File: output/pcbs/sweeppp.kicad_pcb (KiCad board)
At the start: 2 copper layers, 136.5 x 111 mm, 57 parts

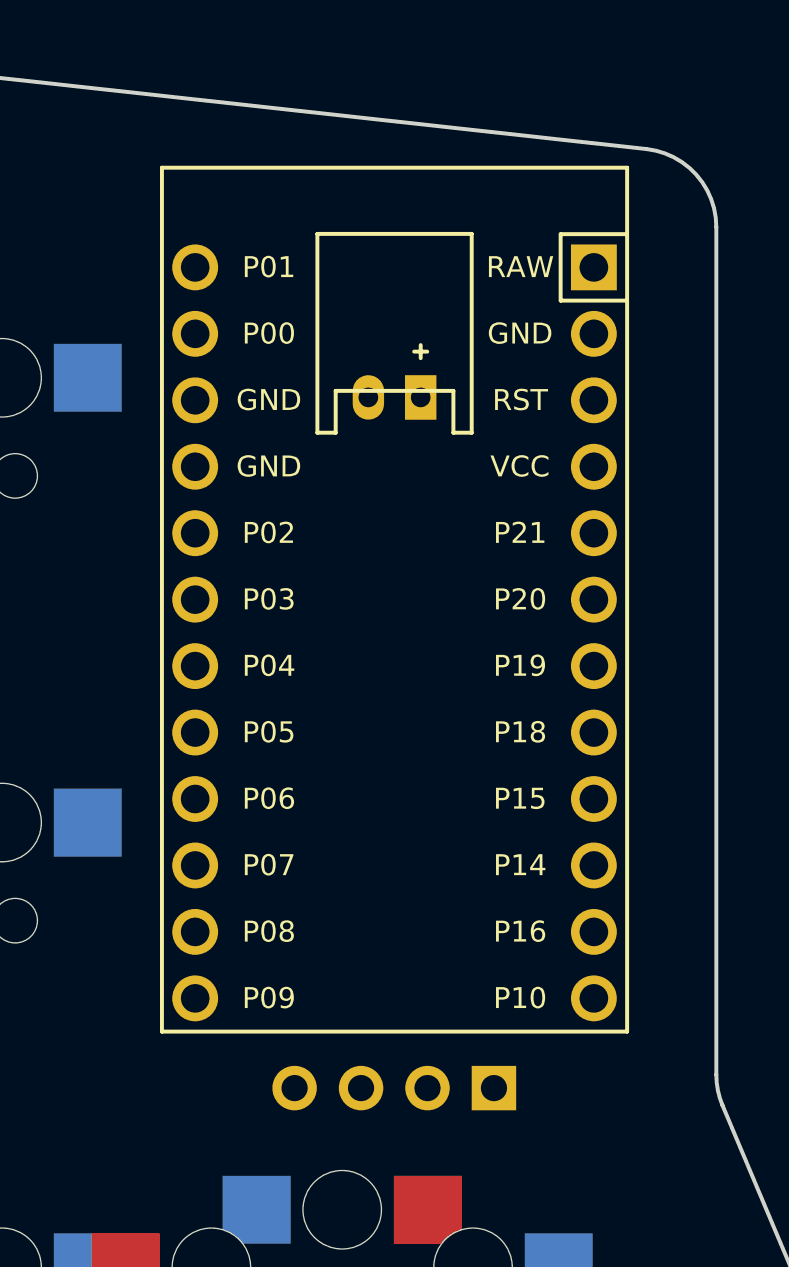
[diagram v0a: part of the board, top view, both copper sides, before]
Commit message: switched to nice nano and nice view
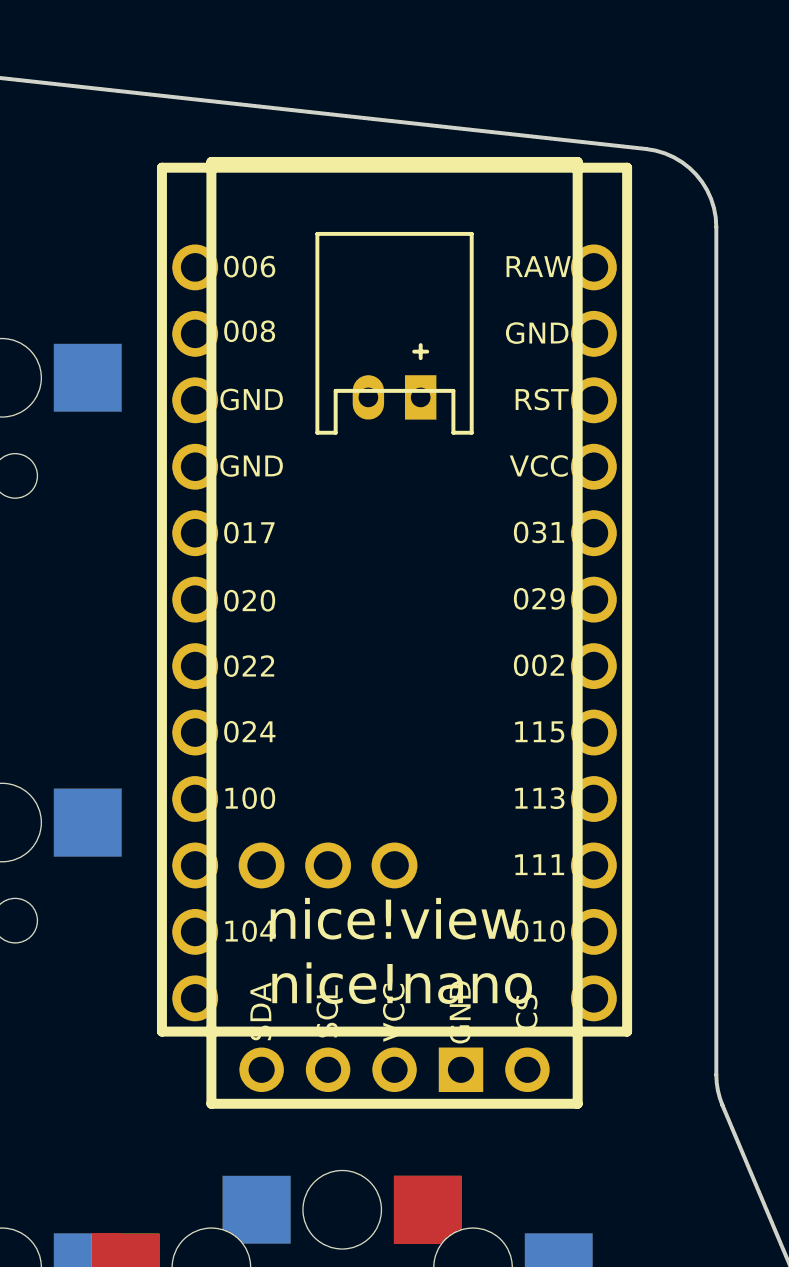
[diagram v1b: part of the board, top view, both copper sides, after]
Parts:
- removed OLED1: OLED, lib:OLED_headers
- added niceView1: niceView, lib:niceView_headers, F.Cu at (192.0, 63.5)
- MCU1: value (none) -> nice_nano; footprint ProMicro -> nice_nano
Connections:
- net P0 renamed P010
- net P1 renamed P009
- net P19 renamed P022
- net P20 renamed P020
- net P21 renamed P017
- MCU1 pad 1: RAW -> P006
- MCU1 pad 10: P14 -> P011
- MCU1 pad 11: P16 -> P104
- MCU1 pad 12: P10 -> P106
- MCU1 pad 15: GND -> P111
- MCU1 pad 16: GND -> P113
- MCU1 pad 17: P2 -> P115
- MCU1 pad 18: P3 -> P002
- MCU1 pad 19: P4 -> P029
- MCU1 pad 2: GND -> P008
- MCU1 pad 20: P5 -> P031
- MCU1 pad 21: P6 -> VCC
- MCU1 pad 22: P7 -> RST
- MCU1 pad 23: P8 -> GND
- MCU1 pad 24: P9 -> RAW
- MCU1 pad 3: RST -> GND
- MCU1 pad 4: VCC -> GND
- MCU1 pad 8: P18 -> P024
- MCU1 pad 9: P15 -> P100

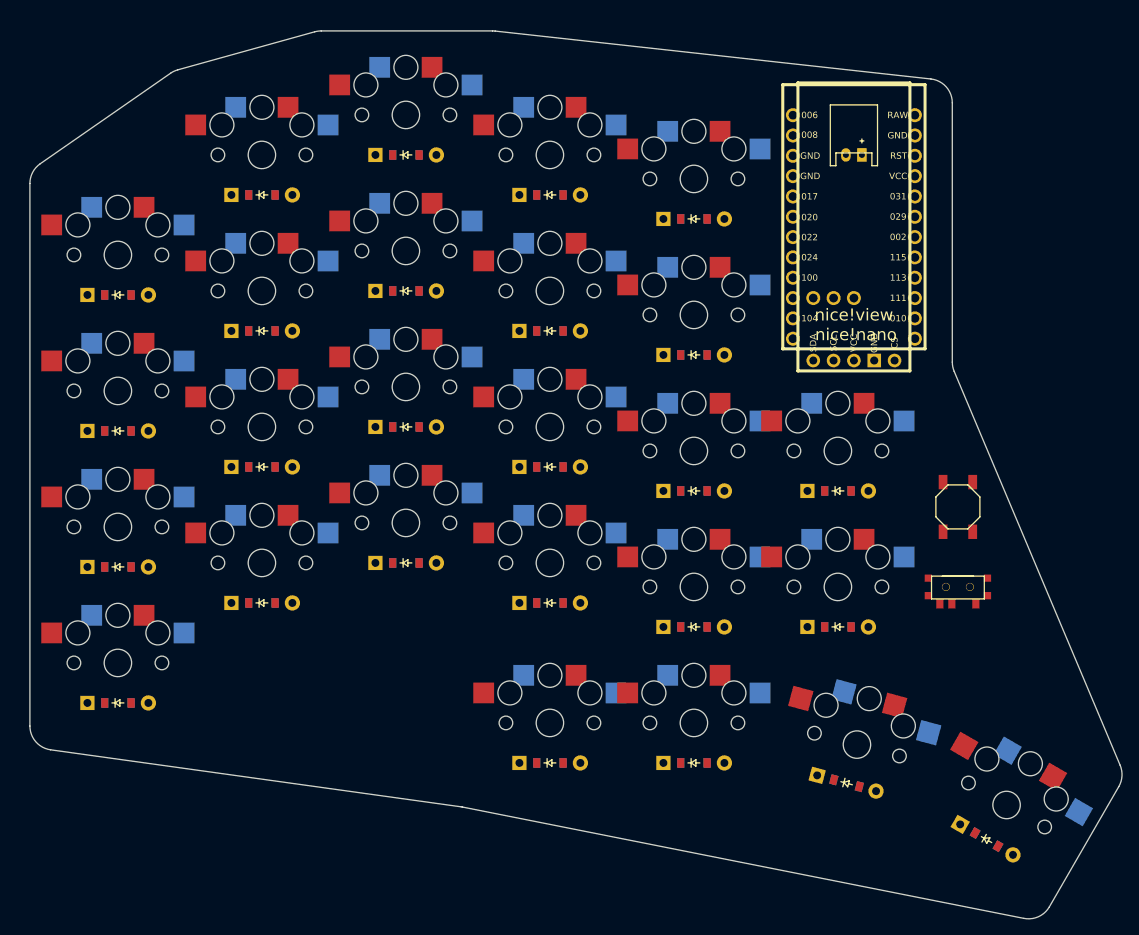
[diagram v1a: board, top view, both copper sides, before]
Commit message: moved the reset button and power switch adjusted outline
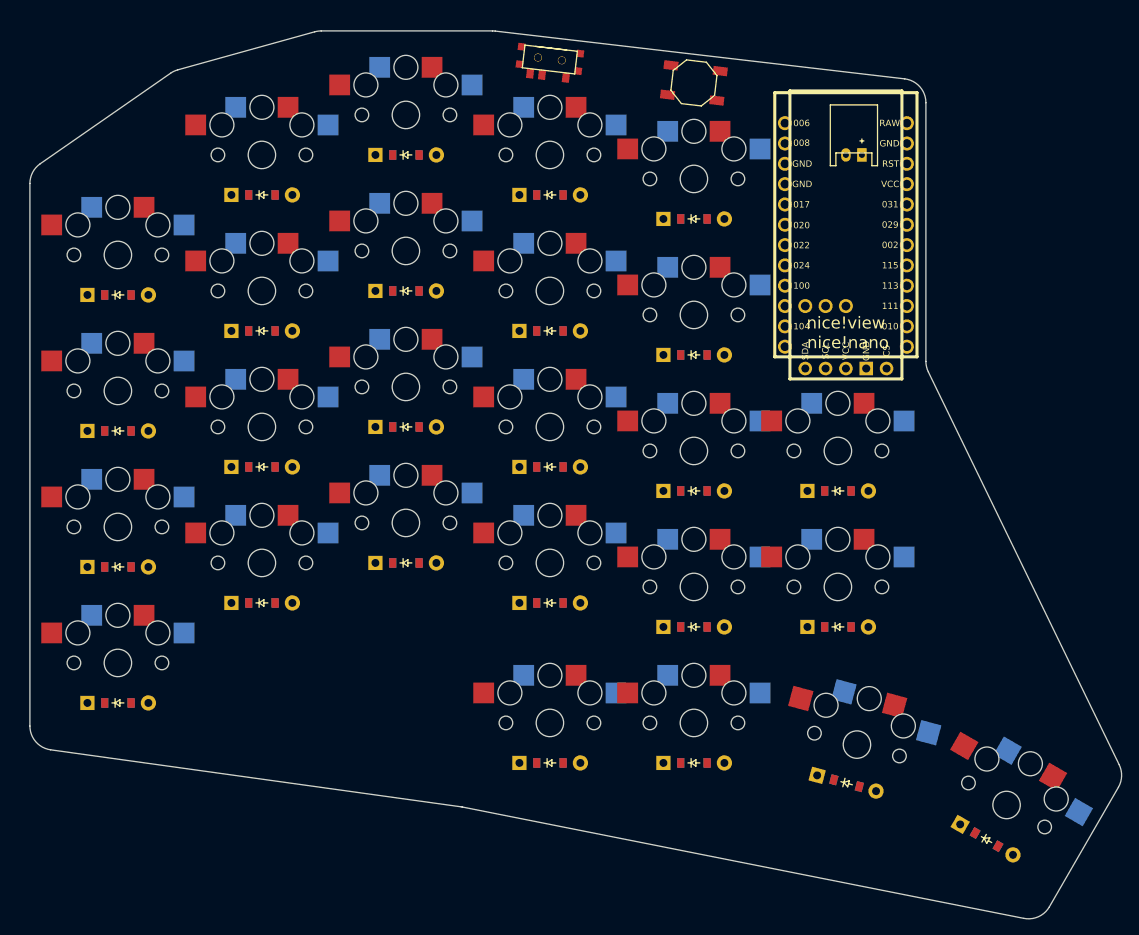
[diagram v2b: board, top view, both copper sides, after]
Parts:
- moved T1 83.4 mm to (154.0, 24.5), turned to -6.7 degrees
- moved B1 62.4 mm to (172.0, 27.5), turned to -6.7 degrees
- moved MCU1 1.41 mm to (191.0, 46.5)
- moved niceView1 1.41 mm to (191.0, 64.5)
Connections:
- D1 pad 1: P4 -> P022
- D10 pad 1: P5 -> P024
- D11 pad 1: P6 -> P100
- D12 pad 1: P7 -> P011
- D13 pad 1: P4 -> P022
- D14 pad 1: P5 -> P024
- D15 pad 1: P6 -> P100
- D16 pad 1: P7 -> P011
- D17 pad 1: P4 -> P022
- D18 pad 1: P5 -> P024
- D19 pad 1: P6 -> P100
- D2 pad 1: P5 -> P024
- D20 pad 1: P7 -> P011
- D21 pad 1: P4 -> P022
- D22 pad 1: P5 -> P024
- D23 pad 1: P8 -> P104
- D24 pad 1: P8 -> P104
- D25 pad 1: P8 -> P104
- D26 pad 1: P8 -> P104
- D3 pad 1: P6 -> P100
- D4 pad 1: P7 -> P011
- D5 pad 1: P4 -> P022
- D6 pad 1: P5 -> P024
- D7 pad 1: P6 -> P100
- D8 pad 1: P7 -> P011
- D9 pad 1: P4 -> P022
- S1 pad 1: P18 -> P115
- S10 pad 1: P14 -> P111
- S11 pad 1: P14 -> P111
- S12 pad 1: P14 -> P111
- S13 pad 1: P16 -> P010
- S14 pad 1: P16 -> P010
- S15 pad 1: P16 -> P010
- S16 pad 1: P16 -> P010
- S17 pad 1: P10 -> P009
- S18 pad 1: P10 -> P009
- S19 pad 1: P10 -> P009
- S2 pad 1: P18 -> P115
- S20 pad 1: P10 -> P009
- S21 pad 1: P9 -> P106
- S22 pad 1: P9 -> P106
- S23 pad 1: P14 -> P111
- S24 pad 1: P16 -> P010
- S25 pad 1: P10 -> P009
- S26 pad 1: P9 -> P106
- S3 pad 1: P18 -> P115
- S4 pad 1: P18 -> P115
- S5 pad 1: P15 -> P113
- S6 pad 1: P15 -> P113
- S7 pad 1: P15 -> P113
- S8 pad 1: P15 -> P113
- S9 pad 1: P14 -> P111
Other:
- outline, holes or cut-outs redrawn

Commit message: moved jstph
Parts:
- moved JST1 79.9 mm to (136.0, 93.5), turned to 0 degrees
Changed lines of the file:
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@@
         (descr "JST PH series connector, S2B-PH-K, side entry type, through hole, Datasheet: http://www.jst-mfg.com/product/pdf/eng/ePH.pdf")
         (tags "connector jst ph")
-        (at 192 36.5 180)
+        (at 136 93.5 0)
         (fp_text reference "JST1" (at 0 0) (layer F.SilkS) hide (effects (font (size 1.27 1.27) (thickness 0.15))))
         (fp_text value "" (at 0 0) (layer F.SilkS) hide (effects (font (size 1.27 1.27) (thickness 0.15))))
@@
         (fp_line (start -1 1.5) (end -1 2.0) (layer F.SilkS) (width 0.15))
         (fp_line (start -1.25 1.75) (end -0.75 1.75) (layer F.SilkS) (width 0.15))
-        (pad 1 thru_hole rect (at -1 0 180) (size 1.2 1.7) (drill 0.75) (layers *.Cu *.Mask) (net 54 "BAT"))
-        (pad 2 thru_hole oval (at 1 0 180) (size 1.2 1.7) (drill 0.75) (layers *.Cu *.Mask) (net 39 "GND"))
+        (pad 1 thru_hole rect (at -1 0 0) (size 1.2 1.7) (drill 0.75) (layers *.Cu *.Mask) (net 54 "BAT"))
+        (pad 2 thru_hole oval (at 1 0 0) (size 1.2 1.7) (drill 0.75) (layers *.Cu *.Mask) (net 39 "GND"))
     )
   (gr_line (start 89 107.88786971388888) (end 89 40.069101149999995) (angle 90) (layer Edge.Cuts) (width 0.15))

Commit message: Added mounting holes
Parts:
- added _1: , MountingHole_2.2mm_M2_Pad_Via, F.Cu at (100.0, 37.0)
- added _2: , MountingHole_2.2mm_M2_Pad_Via, F.Cu at (112.0, 109.0)
- added _3: , MountingHole_2.2mm_M2_Pad_Via, F.Cu at (179.0, 28.5)
- added _4: , MountingHole_2.2mm_M2_Pad_Via, F.Cu at (206.0, 102.5)
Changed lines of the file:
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@@
         (pad 2 thru_hole oval (at 1 0 0) (size 1.2 1.7) (drill 0.75) (layers *.Cu *.Mask) (net 39 "GND"))
+    )
+    (module "MountingHole_2.2mm_M2_Pad_Via" (version 20210722) (generator pcbnew) (layer "F.Cu")
+      (at 100 37 0)
+      (fp_text reference "_1" (at 0 -3.2) (layer "F.SilkS") hide
+        (effects (font (size 1 1) (thickness 0.15)))
+      )
+      (fp_circle (center 0 0) (end 2.45 0) (layer "F.CrtYd") (width 0.05) (fill none))
+      (pad "1" thru_hole circle locked (at 1.166726 1.166726) (size 0.7 0.7) (drill 0.4) (layers *.Cu *.Mask))
+      (pad "1" thru_hole circle locked (at 0 0) (size 4.4 4.4) (drill 2.2) (layers *.Cu *.Mask))
+      (pad "1" thru_hole circle locked (at 0 1.65) (size 0.7 0.7) (drill 0.4) (layers *.Cu *.Mask))
+      (pad "1" thru_hole circle locked (at 1.166726 -1.166726) (size 0.7 0.7) (drill 0.4) (layers *.Cu *.Mask))
+      (pad "1" thru_hole circle locked (at -1.65 0) (size 0.7 0.7) (drill 0.4) (layers *.Cu *.Mask))
+      (pad "1" thru_hole circle locked (at -1.166726 -1.166726) (size 0.7 0.7) (drill 0.4) (layers *.Cu *.Mask))
+      (pad "1" thru_hole circle locked (at -1.166726 1.166726) (size 0.7 0.7) (drill 0.4) (layers *.Cu *.Mask))
+      (pad "1" thru_hole circle locked (at 1.65 0) (size 0.7 0.7) (drill 0.4) (layers *.Cu *.Mask))
+      (pad "1" thru_hole circle locked (at 0 -1.65) (size 0.7 0.7) (drill 0.4) (layers *.Cu *.Mask))
+    )
+    (module "MountingHole_2.2mm_M2_Pad_Via" (version 20210722) (generator pcbnew) (layer "F.Cu")
+      (at 112 109 0)
+      (fp_text reference "_2" (at 0 -3.2) (layer "F.SilkS") hide
+        (effects (font (size 1 1) (thickness 0.15)))
+      )
+      (fp_circle (center 0 0) (end 2.45 0) (layer "F.CrtYd") (width 0.05) (fill none))
+      (pad "1" thru_hole circle locked (at 1.166726 1.166726) (size 0.7 0.7) (drill 0.4) (layers *.Cu *.Mask))
+      (pad "1" thru_hole circle locked (at 0 0) (size 4.4 4.4) (drill 2.2) (layers *.Cu *.Mask))
+      (pad "1" thru_hole circle locked (at 0 1.65) (size 0.7 0.7) (drill 0.4) (layers *.Cu *.Mask))
+      (pad "1" thru_hole circle locked (at 1.166726 -1.166726) (size 0.7 0.7) (drill 0.4) (layers *.Cu *.Mask))
+      (pad "1" thru_hole circle locked (at -1.65 0) (size 0.7 0.7) (drill 0.4) (layers *.Cu *.Mask))
+      (pad "1" thru_hole circle locked (at -1.166726 -1.166726) (size 0.7 0.7) (drill 0.4) (layers *.Cu *.Mask))
+      (pad "1" thru_hole circle locked (at -1.166726 1.166726) (size 0.7 0.7) (drill 0.4) (layers *.Cu *.Mask))
+      (pad "1" thru_hole circle locked (at 1.65 0) (size 0.7 0.7) (drill 0.4) (layers *.Cu *.Mask))
+      (pad "1" thru_hole circle locked (at 0 -1.65) (size 0.7 0.7) (drill 0.4) (layers *.Cu *.Mask))
+    )
+    (module "MountingHole_2.2mm_M2_Pad_Via" (version 20210722) (generator pcbnew) (layer "F.Cu")
+      (at 179 28.5 0)
+      (fp_text reference "_3" (at 0 -3.2) (layer "F.SilkS") hide
+        (effects (font (size 1 1) (thickness 0.15)))
+      )
+      (fp_circle (center 0 0) (end 2.45 0) (layer "F.CrtYd") (width 0.05) (fill none))
+      (pad "1" thru_hole circle locked (at 1.166726 1.166726) (size 0.7 0.7) (drill 0.4) (layers *.Cu *.Mask))
+      (pad "1" thru_hole circle locked (at 0 0) (size 4.4 4.4) (drill 2.2) (layers *.Cu *.Mask))
+      (pad "1" thru_hole circle locked (at 0 1.65) (size 0.7 0.7) (drill 0.4) (layers *.Cu *.Mask))
+      (pad "1" thru_hole circle locked (at 1.166726 -1.166726) (size 0.7 0.7) (drill 0.4) (layers *.Cu *.Mask))
+      (pad "1" thru_hole circle locked (at -1.65 0) (size 0.7 0.7) (drill 0.4) (layers *.Cu *.Mask))
+      (pad "1" thru_hole circle locked (at -1.166726 -1.166726) (size 0.7 0.7) (drill 0.4) (layers *.Cu *.Mask))
+      (pad "1" thru_hole circle locked (at -1.166726 1.166726) (size 0.7 0.7) (drill 0.4) (layers *.Cu *.Mask))
+      (pad "1" thru_hole circle locked (at 1.65 0) (size 0.7 0.7) (drill 0.4) (layers *.Cu *.Mask))
+      (pad "1" thru_hole circle locked (at 0 -1.65) (size 0.7 0.7) (drill 0.4) (layers *.Cu *.Mask))
+    )
+    (module "MountingHole_2.2mm_M2_Pad_Via" (version 20210722) (generator pcbnew) (layer "F.Cu")
+      (at 206 102.5 0)
+      (fp_text reference "_4" (at 0 -3.2) (layer "F.SilkS") hide
+        (effects (font (size 1 1) (thickness 0.15)))
+      )
+      (fp_circle (center 0 0) (end 2.45 0) (layer "F.CrtYd") (width 0.05) (fill none))
+      (pad "1" thru_hole circle locked (at 1.166726 1.166726) (size 0.7 0.7) (drill 0.4) (layers *.Cu *.Mask))
+      (pad "1" thru_hole circle locked (at 0 0) (size 4.4 4.4) (drill 2.2) (layers *.Cu *.Mask))
+      (pad "1" thru_hole circle locked (at 0 1.65) (size 0.7 0.7) (drill 0.4) (layers *.Cu *.Mask))
+      (pad "1" thru_hole circle locked (at 1.166726 -1.166726) (size 0.7 0.7) (drill 0.4) (layers *.Cu *.Mask))
+      (pad "1" thru_hole circle locked (at -1.65 0) (size 0.7 0.7) (drill 0.4) (layers *.Cu *.Mask))
+      (pad "1" thru_hole circle locked (at -1.166726 -1.166726) (size 0.7 0.7) (drill 0.4) (layers *.Cu *.Mask))
+      (pad "1" thru_hole circle locked (at -1.166726 1.166726) (size 0.7 0.7) (drill 0.4) (layers *.Cu *.Mask))
+      (pad "1" thru_hole circle locked (at 1.65 0) (size 0.7 0.7) (drill 0.4) (layers *.Cu *.Mask))
+      (pad "1" thru_hole circle locked (at 0 -1.65) (size 0.7 0.7) (drill 0.4) (layers *.Cu *.Mask))
     )
   (gr_line (start 89 107.88786971388888) (end 89 40.069101149999995) (angle 90) (layer Edge.Cuts) (width 0.15))

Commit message: Added pins for nice!view
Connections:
- niceView1 pad 1: (no net) -> P002
- niceView1 pad 4: P3 -> P020
- niceView1 pad 5: P2 -> P017
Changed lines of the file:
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@@
 (net 50 "P102")
 (net 51 "P107")
-(net 52 "P2")
-(net 53 "P3")
-(net 54 "BAT")
+(net 52 "BAT")
   (net_class Default "This is the default net class."
     (clearance 0.2)
@@
 (add_net "P102")
 (add_net "P107")
-(add_net "P2")
-(add_net "P3")
 (add_net "BAT")
   )
@@
         (fp_text user CS (at 3.5 5.08 270) (layer B.SilkS) (effects (font (size 0.8 0.8) (thickness 0.15)) (justify mirror)))
         (fp_text user nice!view (at 7 0 360) (layer F.SilkS) (effects (font (size 1.5 1.5) (thickness 0.3))))
-        (pad 5 thru_hole oval (at 1.3 -5.08 360) (size 1.7 1.7) (drill 1) (layers *.Cu *.Mask) (net 52 "P2"))
-        (pad 4 thru_hole oval (at 1.3 -2.54 360) (size 1.7 1.7) (drill 1) (layers *.Cu *.Mask) (net 53 "P3"))
+        (pad 5 thru_hole oval (at 1.3 -5.08 360) (size 1.7 1.7) (drill 1) (layers *.Cu *.Mask) (net 47 "P017"))
+        (pad 4 thru_hole oval (at 1.3 -2.54 360) (size 1.7 1.7) (drill 1) (layers *.Cu *.Mask) (net 48 "P020"))
         (pad 3 thru_hole oval (at 1.3 0.00 360) (size 1.7 1.7) (drill 1) (layers *.Cu *.Mask) (net 41 "VCC"))
         (pad 2 thru_hole rect (at 1.3 2.54 360) (size 1.7 1.7) (drill 1) (layers *.Cu *.Mask) (net 39 "GND"))
-        (pad 1 thru_hole oval (at 1.3 5.08 360) (size 1.7 1.7) (drill 1) (layers *.Cu *.Mask) (net 0 ""))
+        (pad 1 thru_hole oval (at 1.3 5.08 360) (size 1.7 1.7) (drill 1) (layers *.Cu *.Mask) (net 44 "P002"))
         )
     (module E73:SW_TACT_ALPS_SKQGABE010 (layer F.Cu)
@@
             (pad "" np_thru_hole circle (at -1.5 0) (size 1 1) (drill 0.9) (layers *.Cu *.Mask))
             (pad 1 smd rect (at 2.25 2.075 -6.7) (size 0.9 1.25) (layers F.Cu F.Paste F.Mask) (net 38 "RAW"))
-            (pad 2 smd rect (at -0.75 2.075 -6.7) (size 0.9 1.25) (layers F.Cu F.Paste F.Mask) (net 54 "BAT"))
+            (pad 2 smd rect (at -0.75 2.075 -6.7) (size 0.9 1.25) (layers F.Cu F.Paste F.Mask) (net 52 "BAT"))
             (pad 3 smd rect (at -2.25 2.075 -6.7) (size 0.9 1.25) (layers F.Cu F.Paste F.Mask))
             (pad "" smd rect (at 3.7 -1.1 -6.7) (size 0.9 0.9) (layers F.Cu F.Paste F.Mask))
@@
         (fp_line (start -1 1.5) (end -1 2.0) (layer F.SilkS) (width 0.15))
         (fp_line (start -1.25 1.75) (end -0.75 1.75) (layer F.SilkS) (width 0.15))
-        (pad 1 thru_hole rect (at -1 0 0) (size 1.2 1.7) (drill 0.75) (layers *.Cu *.Mask) (net 54 "BAT"))
+        (pad 1 thru_hole rect (at -1 0 0) (size 1.2 1.7) (drill 0.75) (layers *.Cu *.Mask) (net 52 "BAT"))
         (pad 2 thru_hole oval (at 1 0 0) (size 1.2 1.7) (drill 0.75) (layers *.Cu *.Mask) (net 39 "GND"))
     )
